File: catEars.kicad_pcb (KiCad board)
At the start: 2 copper layers, 41.3 x 41.4 mm, 26 parts, among them J1 Conn_01x03_Socket, J2 Conn_01x03_Socket, U1 ESP-01v090, U2 AMS1117-3.3

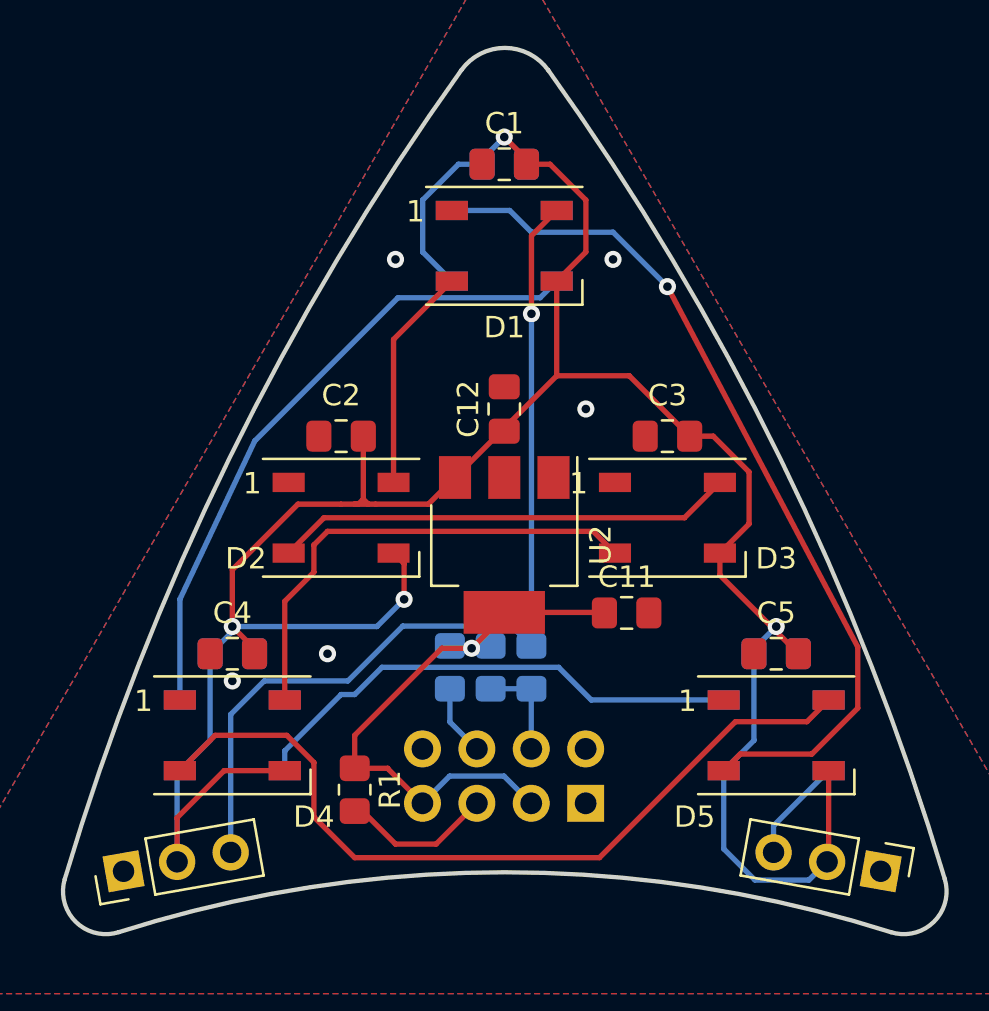
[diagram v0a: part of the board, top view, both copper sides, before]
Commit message: fixed WS2812 VSS VDD
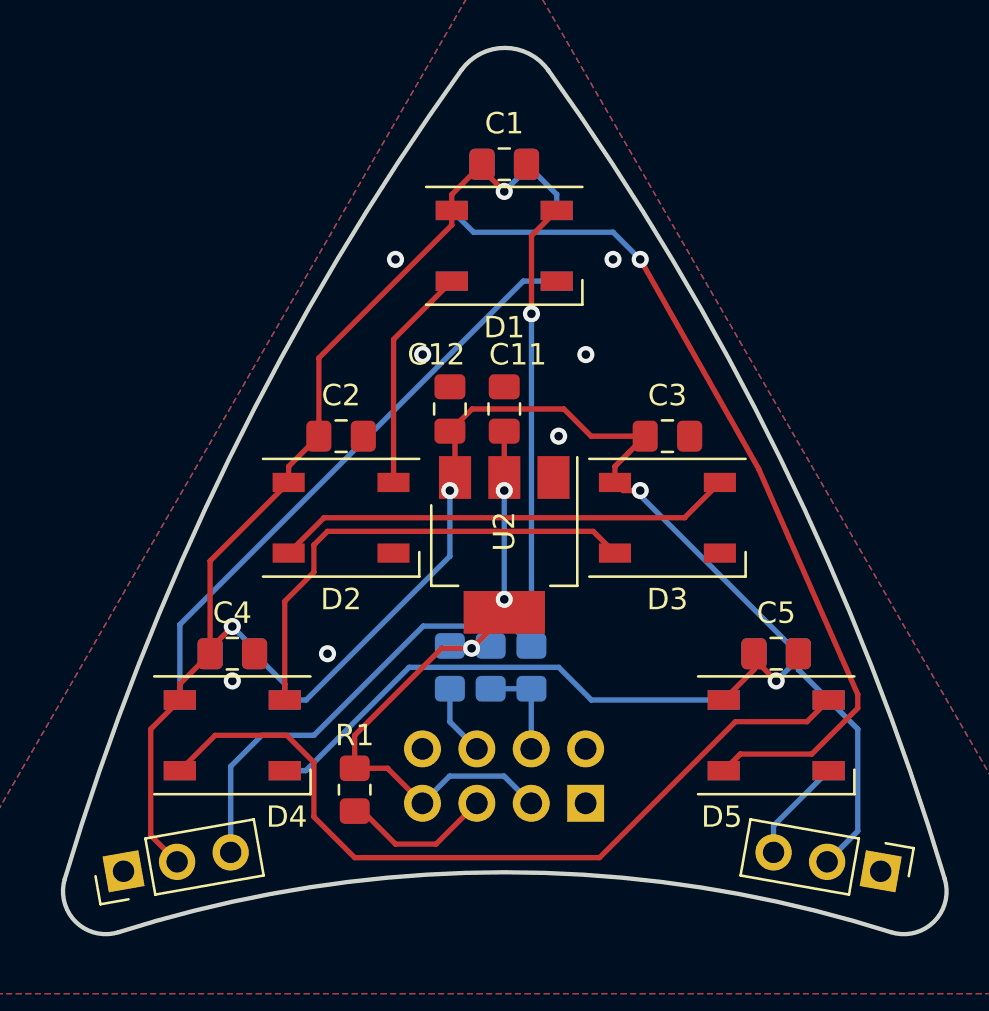
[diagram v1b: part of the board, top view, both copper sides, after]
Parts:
- moved C11 11.1 mm to (58.4, 55.9), turned to 90 degrees
- moved C12 2.54 mm to (55.9, 55.9)
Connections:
- C1 pad 1: +5V -> GND
- C1 pad 2: GND -> +5V
- C2 pad 1: +5V -> GND
- C2 pad 2: GND -> +5V
- C3 pad 1: +5V -> GND
- C3 pad 2: GND -> +5V
- C4 pad 1: +5V -> GND
- C4 pad 2: GND -> +5V
- C5 pad 1: +5V -> GND
- C5 pad 2: GND -> +5V
- C6 pad 1: +5V -> GND
- C6 pad 2: GND -> +5V
- C7 pad 1: +5V -> GND
- C7 pad 2: GND -> +5V
- C8 pad 1: +5V -> GND
- C8 pad 2: GND -> +5V
- D1 pad 1: GND -> +5V
- D1 pad 3: +5V -> GND
- D2 pad 1: GND -> +5V
- D2 pad 3: +5V -> GND
- D3 pad 1: GND -> +5V
- D3 pad 3: +5V -> GND
- D4 pad 1: GND -> +5V
- D4 pad 3: +5V -> GND
- D5 pad 1: GND -> +5V
- D5 pad 3: +5V -> GND
- D6 pad 1: GND -> +5V
- D6 pad 3: +5V -> GND
- D7 pad 1: GND -> +5V
- D7 pad 3: +5V -> GND
- D8 pad 1: GND -> +5V
- D8 pad 3: +5V -> GND
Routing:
- net +5V: track 124.5 -> 110.1 mm, vias 4 -> 5
- net 3V3: track 29.6 -> 32.1 mm, vias 1 -> 3
- net Net-(D6-DOUT): track 30.1 -> 27.8 mm
- net LED: track 43.4 -> 42.0 mm
- net Net-(D7-DOUT): track 23.7 -> 23.1 mm
- net GND: vias 5 -> 7

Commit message: some optimisations
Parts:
- R1: moved to B.Cu
- moved R1 6.87 mm to (55.2, 67.9)
- moved R3 1.27 mm to (59.1, 67.9)
- moved R4 1.27 mm to (61.0, 67.9)
- moved R2 1.27 mm to (57.1, 67.9)
- renumbered R4 to R2, R2 to R4
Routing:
- net 3V3: track 32.1 -> 34.0 mm
- net Net-(U1-RST): track 7.28 -> 6.13 mm
- net Net-(U1-GPIO0): track 3.33 -> 2.81 mm

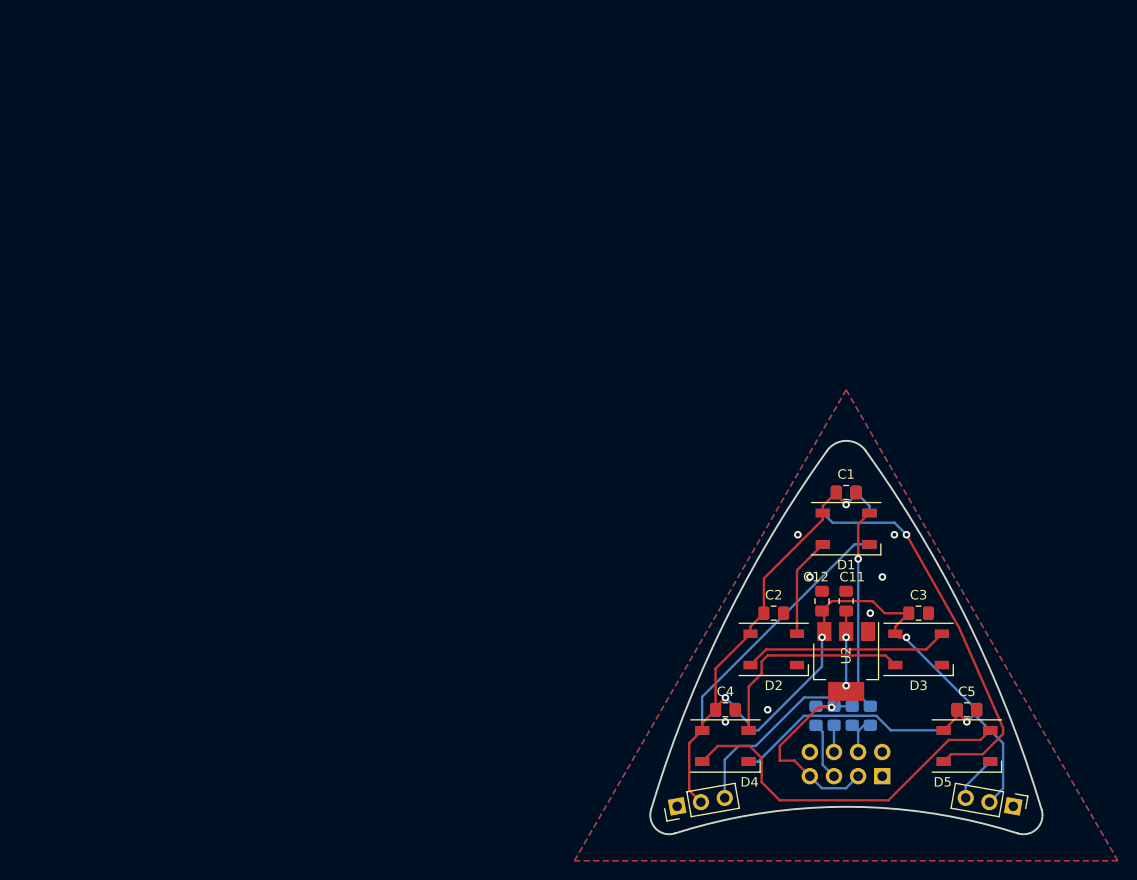
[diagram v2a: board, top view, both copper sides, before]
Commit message: moved PCB to origin
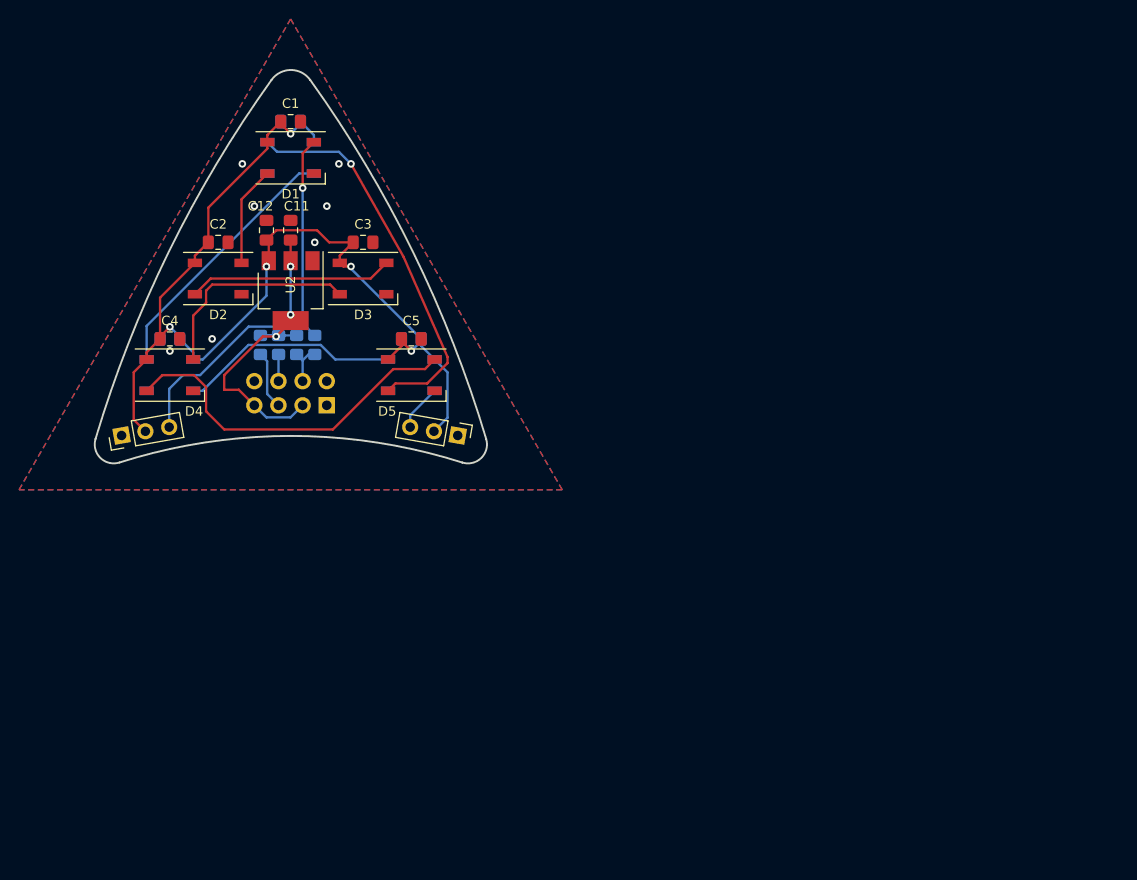
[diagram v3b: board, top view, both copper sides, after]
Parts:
- moved C1 70.3 mm to (-0.02, 5.43)
- moved C11 70.3 mm to (-0.02, 16.9)
- moved C12 70.3 mm to (-2.56, 16.9)
- moved C3 70.3 mm to (7.60, 18.1)
- moved C5 70.3 mm to (12.7, 28.3)
- moved C6 70.3 mm to (-0.02, 5.43)
- moved C8 70.3 mm to (12.7, 28.3)
- moved D1 70.3 mm to (-0.02, 9.24)
- moved D3 70.3 mm to (7.60, 21.9)
- moved D5 70.3 mm to (12.7, 32.1)
- moved D6 70.3 mm to (-0.02, 9.24)
- moved D8 70.3 mm to (12.7, 32.1)
- moved J1 70.3 mm to (-17.8, 38.5)
- moved J2 70.3 mm to (17.6, 38.5)
- moved R2 70.3 mm to (-1.29, 28.9)
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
